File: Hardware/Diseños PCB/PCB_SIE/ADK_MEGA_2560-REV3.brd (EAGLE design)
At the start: 1 x 1 mm, 29 parts

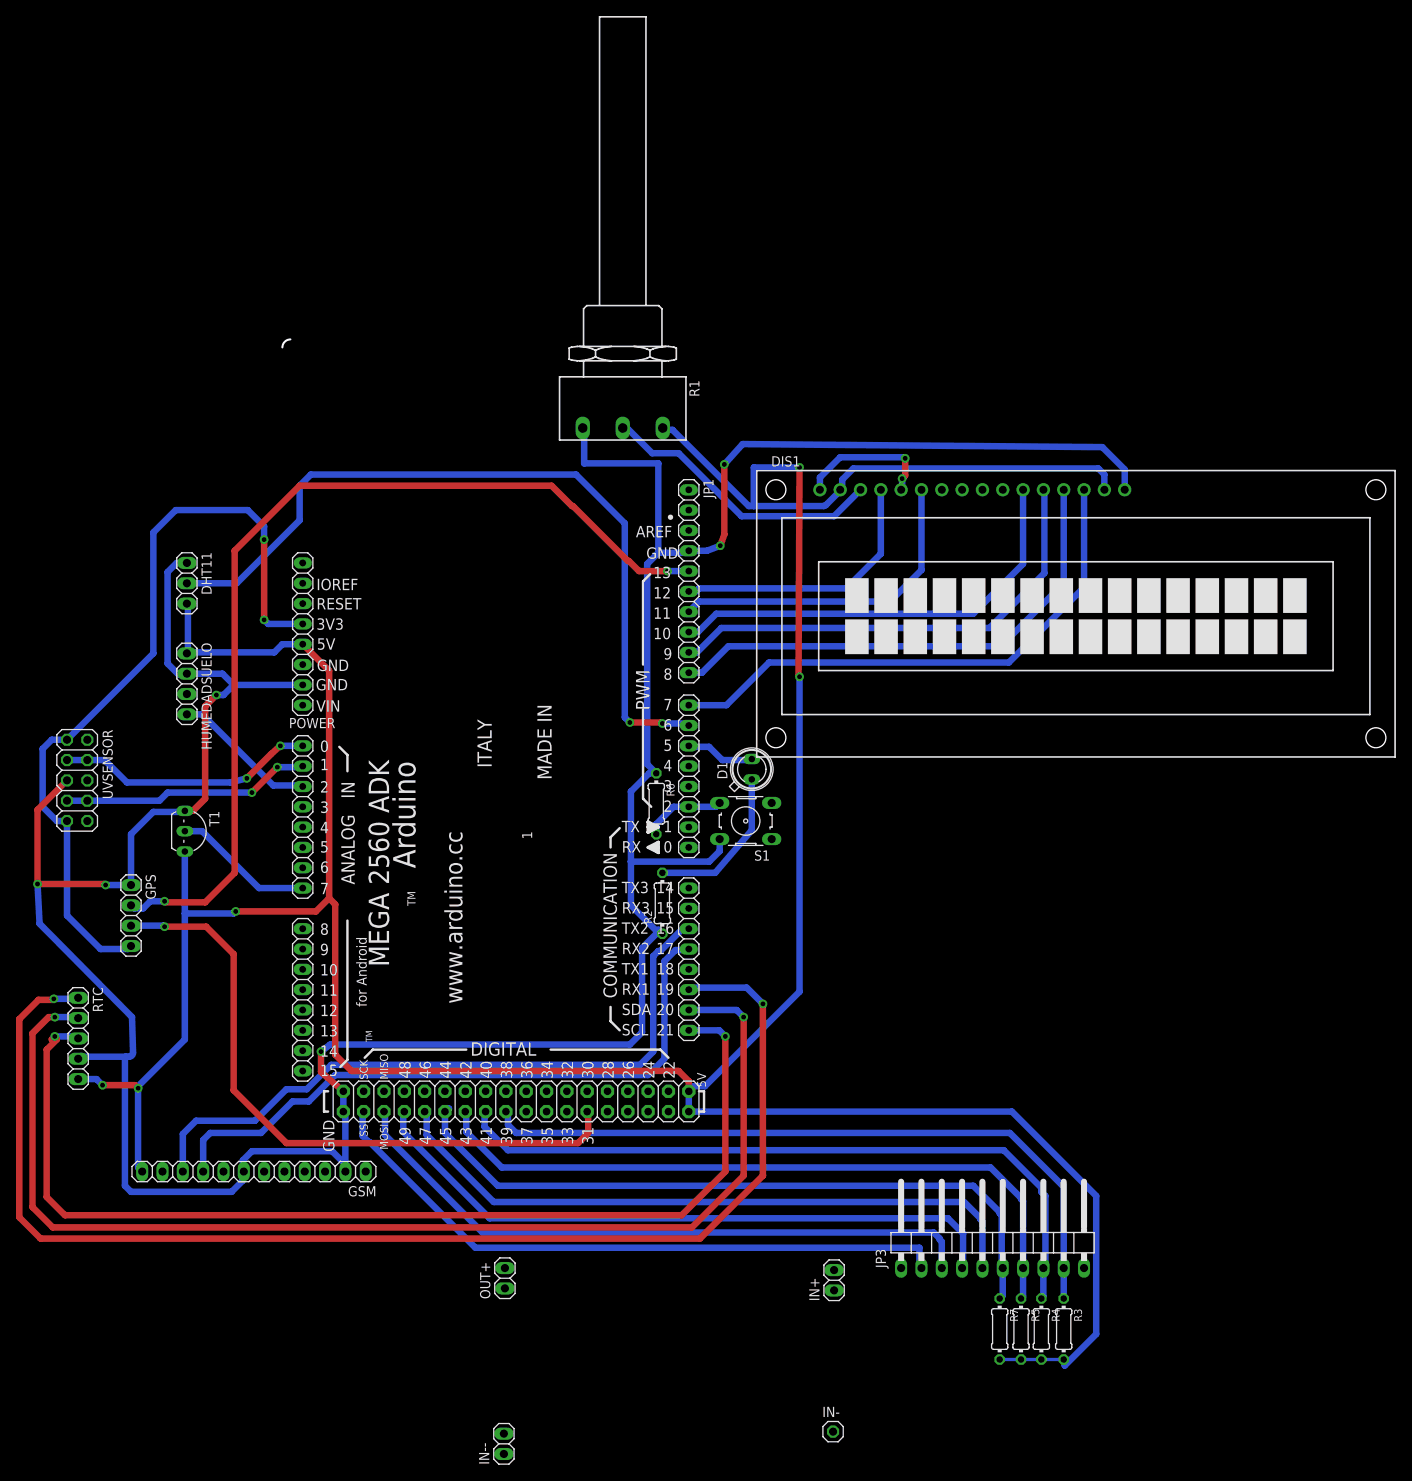
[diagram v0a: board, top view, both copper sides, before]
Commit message: Se modifica la posicion del GPS, se corrijen paths y se distancian sensores
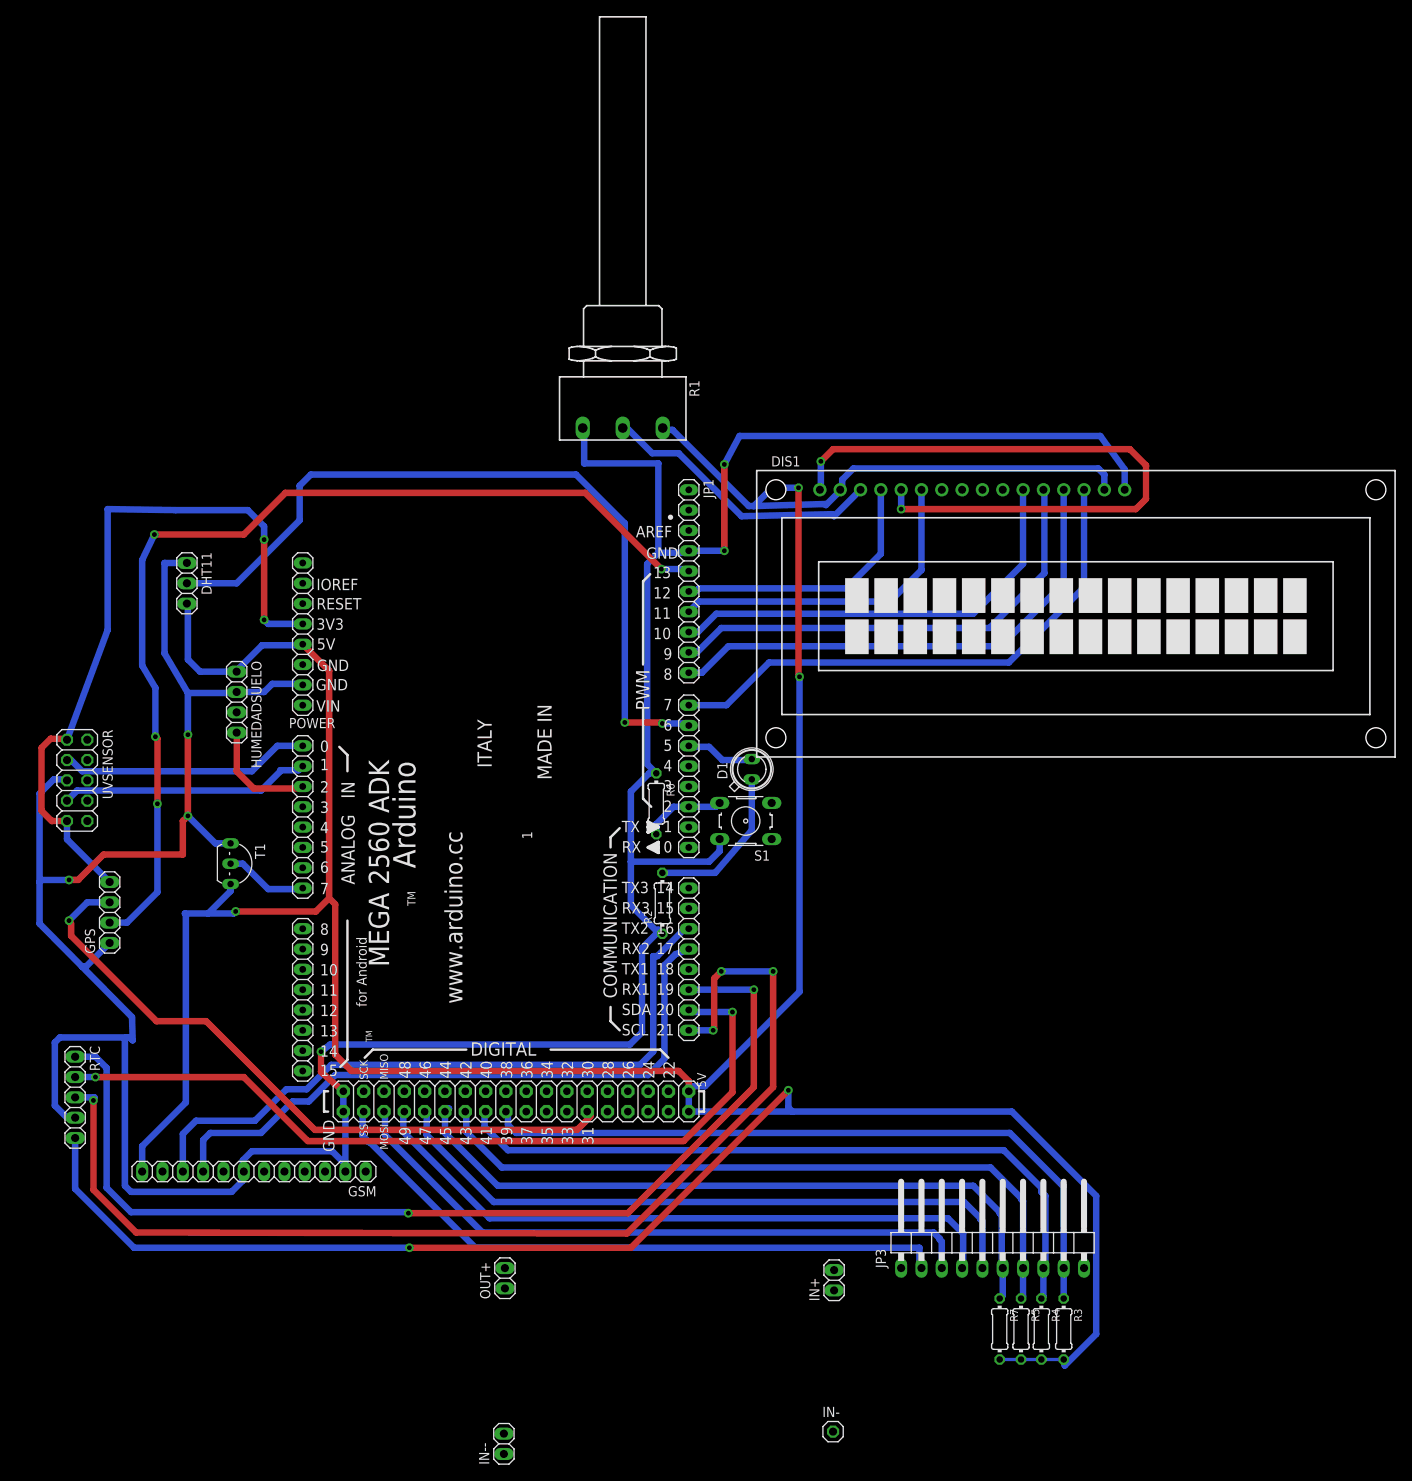
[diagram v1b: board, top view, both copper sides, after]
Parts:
- moved RTC 7.38 mm to (-22.4, 7.24)
- moved T1 7.01 mm to (-1.65, 36.4)
- moved HUMEDADSUELO 6.63 mm to (-2.16, 56.6)
- moved GPS 2.69 mm to (-18.0, 30.4), turned to 90 degrees
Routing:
- net VCC: track 439.3 -> 533.4 mm
- net N$5: track 17.4 -> 83.5 mm
- net N$15: track 148.0 -> 103.6 mm
- net N$16: track 162.6 -> 128.6 mm
- net GND: track 411.4 -> 438.1 mm
- net N$18: track 17.7 -> 10.4 mm
- net N$29: track 99.2 -> 92.0 mm
- net N$14: track 134.2 -> 140.5 mm, vias 2 -> 4
- net N$11: track 119.9 -> 126.2 mm, vias 2 -> 4
- net N$17: track 18.2 -> 14.1 mm
- net N$13: track 81.6 -> 84.4 mm
- net N$20: track 32.3 -> 31.4 mm, vias 2 -> 0
- net N$19: track 31.4 -> 31.7 mm, vias 2 -> 0
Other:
- board outline removed
